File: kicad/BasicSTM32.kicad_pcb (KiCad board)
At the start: 4 copper layers, 61 parts, among them IC1 TPSM53604RDAR, IC2 LD39100PU33R, J1 Screw_Terminal_01x02, J10 Conn_01x04, J11 TC2050-IDC, J2 Conn_01x01, J3 Conn_01x01, J4 Conn_01x02, J5 Conn_01x01, J6 Conn_01x02, J7 DAC1_OUT1, J8 ADC1_IN1, J9 GPIO_OUT PB15, Q1 SI2374DS-T1-GE3, Q2 SI2374DS-T1-GE3, SW1 SW_Push, U1 STM32F303VETx, Y1 NX3225GD-8MHZ-EXS00A-CG04874

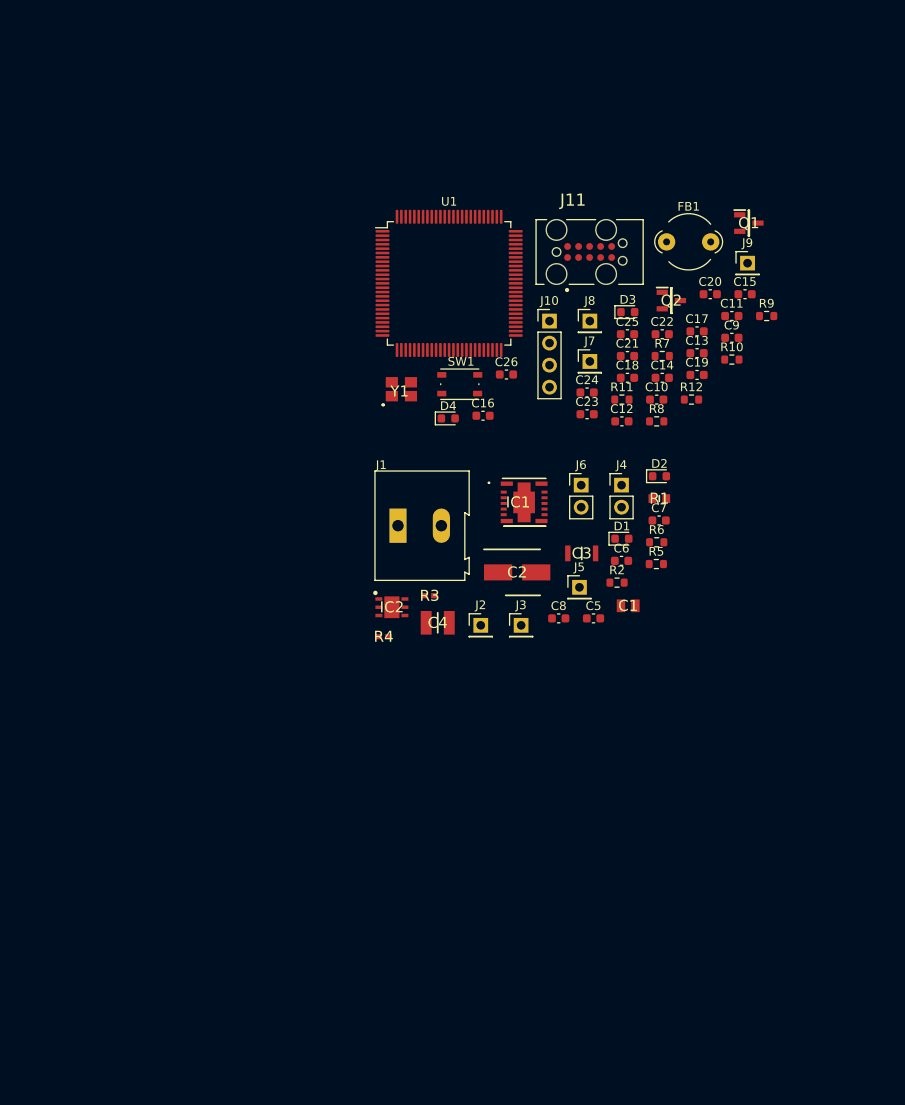
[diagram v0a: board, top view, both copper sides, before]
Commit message: Power supply layout
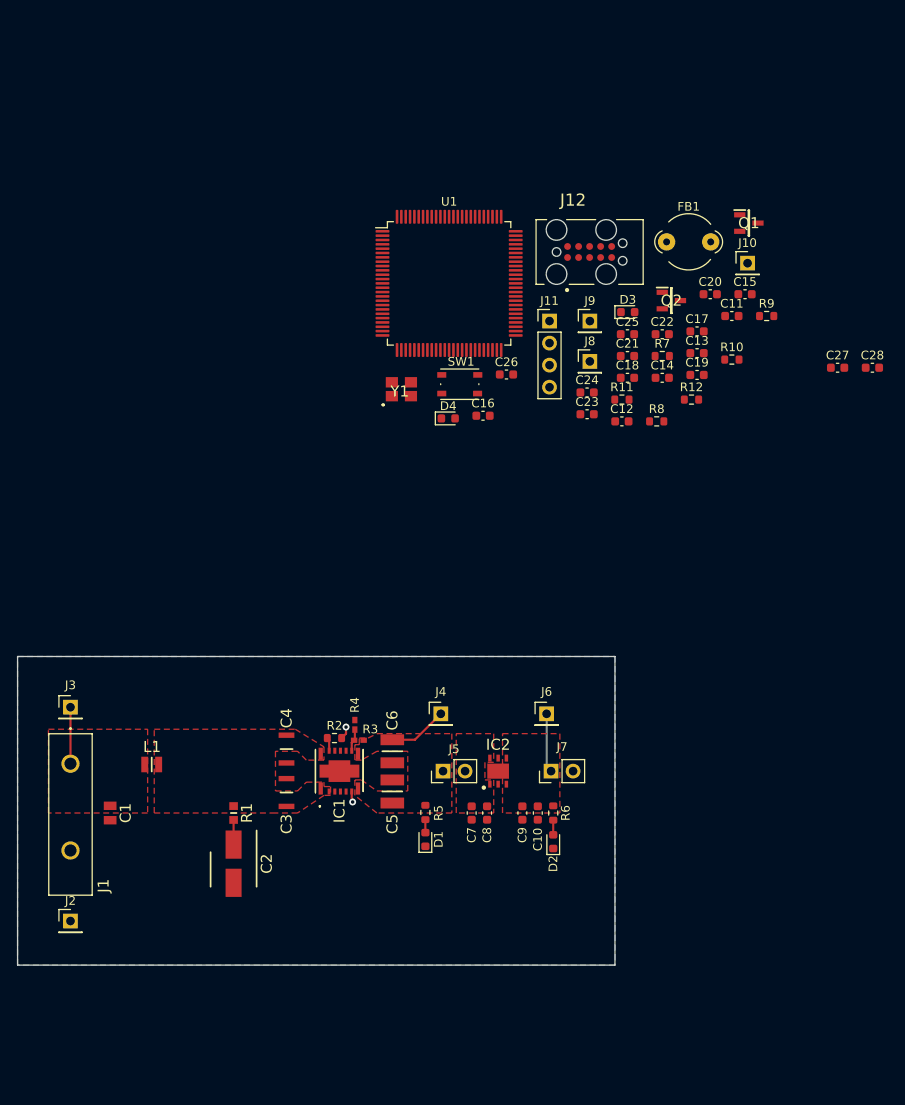
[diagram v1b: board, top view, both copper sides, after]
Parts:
- added C27: 100n, Capacitor_SMD:C_0603_1608Metric, F.Cu at (142.7, 73.4)
- added C28: 1u, Capacitor_SMD:C_0603_1608Metric, F.Cu at (146.8, 73.4)
- added J2: Conn_01x01, Connector_PinHeader_2.54mm:PinHeader_1x01_P2.54mm_Vertical, F.Cu at (54.4, 137.2)
- added L1: DFE201612P-R33M=P2, SamacSys_Parts:1286ASH1R0MP2, F.Cu at (63.7, 119.1)
- C11: value 1u -> 100n
- C12: value 4.7u -> 100n
- C13, C19, C9: value 100n -> 1u
- C14: value 100n -> 4.7u
- C15, C16: value 4.3p -> 100n
- C17, C18: value 1u -> 4.3p
- C4: value GRM32EC81C476KE15L -> C3216X5R1H106K160AB; footprint SamacSys_Parts:CAPC3225X270N -> SamacSys_Parts:CAPC3216X180N
- C5: value 1u -> GRM32EC81C476KE15L; footprint Capacitor_SMD:C_0603_1608Metric -> SamacSys_Parts:CAPC3225X270N
- C6: value 100n -> GRM32EC81C476KE15L; footprint Capacitor_SMD:C_0603_1608Metric -> SamacSys_Parts:CAPC3225X270N
- J1: value Screw_Terminal_01x02 -> 1935161; footprint TerminalBlock:TerminalBlock_Altech_AK300-2_P5.00mm -> SamacSys_Parts:1701023
- moved C1 64.3 mm to (58.9, 124.7), turned to 270 degrees
- moved R1 61.0 mm to (73.2, 124.7), turned to 270 degrees
- moved C9 59.8 mm to (106.4, 124.7), turned to 270 degrees
- moved C10 49.6 mm to (108.2, 124.7), turned to 270 degrees
- moved J3 48.2 mm to (54.4, 112.5)
- moved C2 46.8 mm to (73.2, 130.6), turned to 270 degrees
- moved J1 46.6 mm to (54.4, 119.0), turned to 180 degrees
- moved D2 43.9 mm to (110.0, 128.0), turned to 90 degrees
- moved C3 43.8 mm to (79.2, 122.4), turned to 90 degrees
- moved D1 41.4 mm to (95.2, 127.8), turned to 90 degrees
- moved C7 40.0 mm to (100.6, 124.7), turned to 270 degrees
- moved R5 39.1 mm to (95.2, 124.7), turned to 270 degrees
- moved J5 38.8 mm to (97.3, 119.9), turned to 90 degrees
- moved IC1 38.2 mm to (85.3, 121.9), turned to 90 degrees
- moved R2 37.2 mm to (84.8, 116.1)
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- renumbered J9 to J10, J10 to J11, J11 to J12, J2 to J3, J3 to J4, J4 to J5, J5 to J6, J6 to J7, J7 to J8, J8 to J9
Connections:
- C10 pad 1: /MCU/NRST -> +3V3
- C12 pad 1: VDD -> /MCU/NRST
- C15 pad 1: GND -> VDD
- C15 pad 2: Net-(C15-Pad2) -> GND
- C16 pad 1: Net-(C16-Pad1) -> VDD
- C17 pad 1: VDD -> GND
- C17 pad 2: GND -> Net-(C17-Pad2)
- C18 pad 1: VDD -> Net-(C18-Pad1)
- C25 pad 1: /MCU/VDDA22 -> VDD
- C26 pad 1: /MCU/VDDA22 -> VDD
- C4 pad 1: +5V -> Net-(C3-Pad1)
- C5 pad 1: Net-(C5-Pad1) -> +5V
- C6 pad 1: Net-(C5-Pad1) -> +5V
- C7 pad 1: +3V3 -> Net-(C7-Pad1)
- C8 pad 1: +3V3 -> Net-(C7-Pad1)
- C9 pad 1: VDD -> +3V3
- IC2 pad 1: Net-(C5-Pad1) -> Net-(C7-Pad1)
- IC2 pad 6: Net-(C5-Pad1) -> Net-(C7-Pad1)
- J1 pad 1: GND -> Net-(C1-Pad1)
- J1 pad 2: Net-(C1-Pad1) -> GND
- J5 pad 2: Net-(C5-Pad1) -> Net-(C7-Pad1)
- U1 pad 12: Net-(C15-Pad2) -> Net-(C17-Pad2)
- U1 pad 13: Net-(C16-Pad1) -> Net-(C18-Pad1)
- Y1 pad 1: Net-(C16-Pad1) -> Net-(C18-Pad1)
- Y1 pad 2: Net-(C15-Pad2) -> Net-(C17-Pad2)
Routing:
- net Net-(IC1-Pad6): track 0.00 -> 11.7 mm, vias 0 -> 2
- net +3V3: track 0.00 -> 7.28 mm
- net +5V: track 0.00 -> 6.83 mm
- net Net-(C1-Pad1): track 0.00 -> 6.51 mm
- net Net-(C2-Pad1): track 0.00 -> 2.84 mm
- net Net-(IC1-Pad9): track 0.00 -> 2.58 mm
- net Net-(D2-Pad2): track 0.00 -> 1.69 mm
- net Net-(IC1-Pad13): track 0.00 -> 1.55 mm
- net Net-(D1-Pad2): track 0.00 -> 1.50 mm
- net GND: track 0.00 -> 0.75 mm
- added copper zone on F.Cu, net +3V3
- added copper zone on F.Cu, net +5V
- added copper zone on B.Cu, net GND
- added copper zone on F.Cu, net Net-(C1-Pad1)
- added copper zone on F.Cu, net Net-(C3-Pad1)
- added copper zone on F.Cu, net Net-(C7-Pad1)
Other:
- board outline added: 68.8 x 35.6 mm

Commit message: Start MCU layout
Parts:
- J11: value Conn_01x04 -> S4B-PH-KL_LF__SN_; footprint Connector_PinHeader_2.54mm:PinHeader_1x04_P2.54mm_Vertical -> SamacSys_Parts:S4BPHKLLFSN
- moved J11 45.3 mm to (71.9, 93.2), turned to 90 degrees
- moved C12 44.7 mm to (88.6, 45.8), turned to 180 degrees
- moved C17 40.5 mm to (86.7, 61.6), turned to 270 degrees
- moved C18 33.1 mm to (86.7, 65.4), turned to 270 degrees
- moved J9 29.4 mm to (85.4, 73.9)
- moved SW1 27.7 mm to (88.6, 49.7), turned to 90 degrees
- moved J8 27.5 mm to (88.1, 81.3)
- moved J12 21.6 mm to (98.2, 45.5), turned to 90 degrees
- moved Y1 14.8 mm to (84.3, 63.5), turned to 90 degrees
- moved C1 14.0 mm to (72.9, 125.0)
- moved J1 14.0 mm to (68.3, 119.0)
- moved J2 14.0 mm to (68.3, 137.2)
- moved J3 14.0 mm to (68.3, 112.5)
- moved L1 10.6 mm to (74.3, 119.4)
- moved C2 3.09 mm to (76.2, 131.1)
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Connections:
- J11 pad 2: GND -> Net-(J11-Pad2)
- J11 pad 3: Net-(J11-Pad3) -> VDD
- J11 pad 4: VDD -> GND
- U1 pad 92: Net-(J11-Pad3) -> Net-(J11-Pad2)
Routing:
- net /MCU/NRST: track 0.00 -> 29.8 mm, vias 0 -> 2
- net Net-(C17-Pad2): track 0.00 -> 5.99 mm
- net Net-(C18-Pad1): track 0.00 -> 5.68 mm
- net Net-(J11-Pad2): track 0.00 -> 3.51 mm, vias 0 -> 1
- net Net-(J11-Pad1): track 0.00 -> 3.51 mm, vias 0 -> 1
- net GND: track 0.75 -> 2.65 mm
- net VDD: track 0.00 -> 1.17 mm, vias 0 -> 1
- net Net-(C2-Pad1): track 2.84 -> 3.40 mm

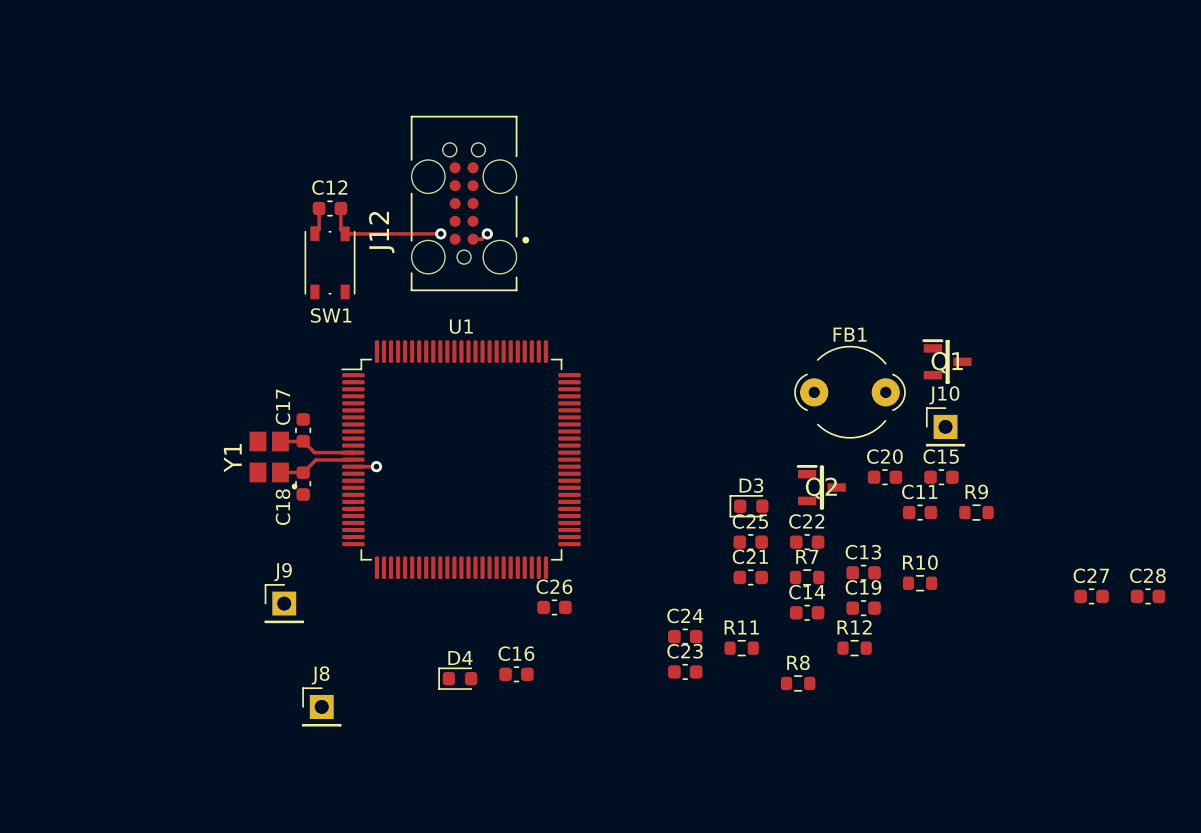
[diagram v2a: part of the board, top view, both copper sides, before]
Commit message: Continue MCU layout
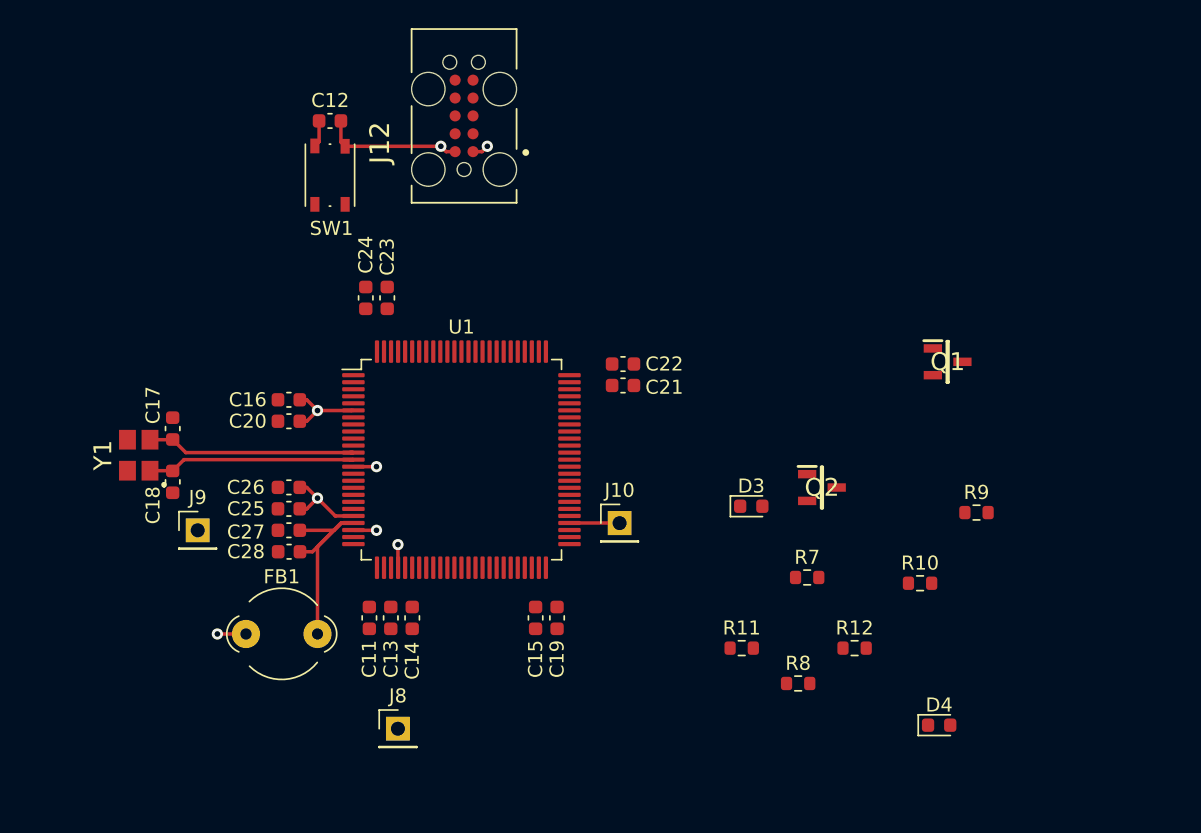
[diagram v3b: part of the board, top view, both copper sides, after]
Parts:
- moved C28 61.1 mm to (85.7, 70.2), turned to 180 degrees
- moved C27 57.2 mm to (85.7, 68.7), turned to 180 degrees
- moved FB1 43.9 mm to (82.7, 76.1)
- moved C20 42.5 mm to (85.7, 61.0), turned to 180 degrees
- moved C11 39.8 mm to (91.4, 74.9), turned to 270 degrees
- moved D4 34.2 mm to (131.9, 82.5)
- moved C23 34.0 mm to (92.7, 52.2), turned to 90 degrees
- moved C13 33.7 mm to (93.0, 74.9), turned to 270 degrees
- moved C24 33.1 mm to (91.2, 52.2), turned to 90 degrees
- moved C25 32.9 mm to (85.7, 67.2), turned to 180 degrees
- moved C15 30.5 mm to (103.3, 74.9), turned to 270 degrees
- moved C14 28.1 mm to (94.5, 74.9), turned to 270 degrees
- moved C16 25.3 mm to (85.7, 59.4), turned to 180 degrees
- moved J10 24.1 mm to (109.2, 68.2)
- moved C19 21.8 mm to (104.8, 74.9), turned to 270 degrees
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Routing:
- net /MCU/VDDA22: track 0.00 -> 16.4 mm
- net Net-(J8-Pad1): track 0.00 -> 14.7 mm, vias 0 -> 1
- net Net-(J9-Pad1): track 0.00 -> 14.3 mm, vias 0 -> 1
- net VDD: track 1.17 -> 15.1 mm, vias 1 -> 4
- net Net-(C18-Pad1): track 5.68 -> 15.1 mm
- net Net-(C17-Pad2): track 5.99 -> 15.3 mm
- net /MCU/NRST: track 29.8 -> 37.1 mm
- net Net-(J10-Pad1): track 0.00 -> 3.57 mm

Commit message: Finish layout first pass
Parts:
- moved Q1 68.2 mm to (88.4, 108.7), turned to 270 degrees
- moved R9 64.3 mm to (88.4, 112.1), turned to 90 degrees
- moved J12 59.4 mm to (108.4, 97.8), turned to 0 degrees
- moved D3 56.9 mm to (88.4, 115.2), turned to 270 degrees
- moved C12 55.2 mm to (114.0, 88.6), turned to 90 degrees
- moved C22 53.3 mm to (95.9, 108.4), turned to 270 degrees
- moved C21 52.3 mm to (94.4, 108.4), turned to 270 degrees
- moved SW1 50.0 mm to (110.2, 88.6), turned to 0 degrees
- moved R7 47.1 mm to (91.7, 107.7), turned to 180 degrees
- moved J10 47.0 mm to (84.6, 108.2), turned to 270 degrees
- moved Q2 45.5 mm to (100.6, 104.9), turned to 270 degrees
- moved D4 42.6 mm to (100.6, 111.4), turned to 270 degrees
- moved C23 40.4 mm to (101.1, 91.7), turned to 0 degrees
- moved R10 40.0 mm to (107.8, 105.4)
- moved C19 39.8 mm to (77.3, 103.8), turned to 180 degrees
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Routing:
- net VDD: track 15.1 -> 47.2 mm, vias 4 -> 12
- net Net-(J12-Pad4): track 0.01 -> 24.2 mm, vias 0 -> 2
- net Net-(J11-Pad2): track 3.51 -> 27.6 mm
- net Net-(J11-Pad1): track 3.51 -> 27.3 mm
- net Net-(J12-Pad2): track 0.00 -> 23.3 mm, vias 0 -> 2
- net /MCU/NRST: track 37.1 -> 54.1 mm, vias 2 -> 3
- net GND: track 2.65 -> 15.9 mm, vias 0 -> 3
- net Net-(Q2-Pad1): track 0.00 -> 7.09 mm
- net Net-(Q1-Pad1): track 0.00 -> 5.08 mm
- net Net-(IC1-Pad6): track 11.7 -> 14.5 mm
- net Net-(Q1-Pad3): track 0.00 -> 1.55 mm
- net Net-(Q2-Pad3): track 0.00 -> 1.55 mm
- net Net-(D3-Pad1): track 0.00 -> 1.46 mm
- net Net-(D4-Pad1): track 0.00 -> 1.46 mm
- net Net-(C3-Pad1): track 0.00 -> 1.12 mm
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- added copper zone on F.Cu, net GND
- added copper zone on GND, net GND
- added copper zone on F.Cu, net VDD
- added copper zone on VDD, net VDD
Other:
- board size 68.8 x 35.6 mm -> 64.3 x 83.2 mm

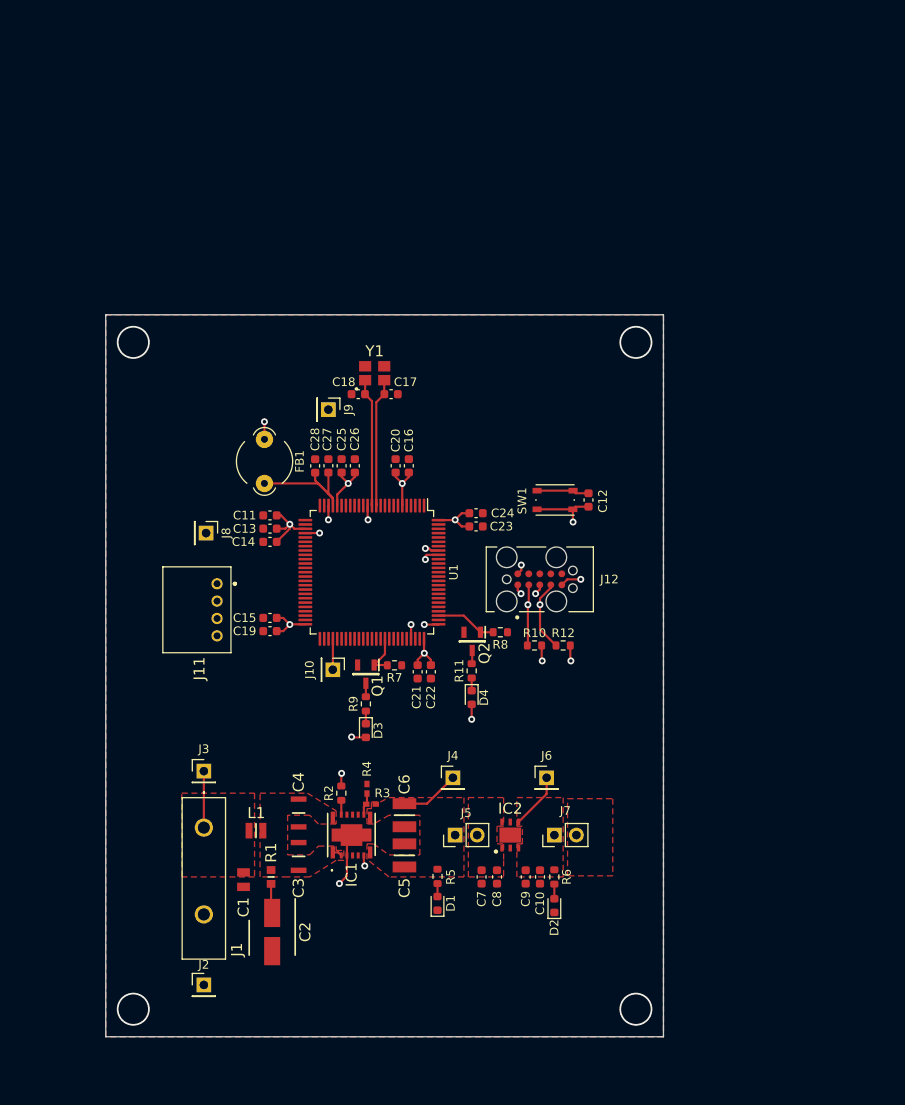
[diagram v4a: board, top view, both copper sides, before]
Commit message: Add USB
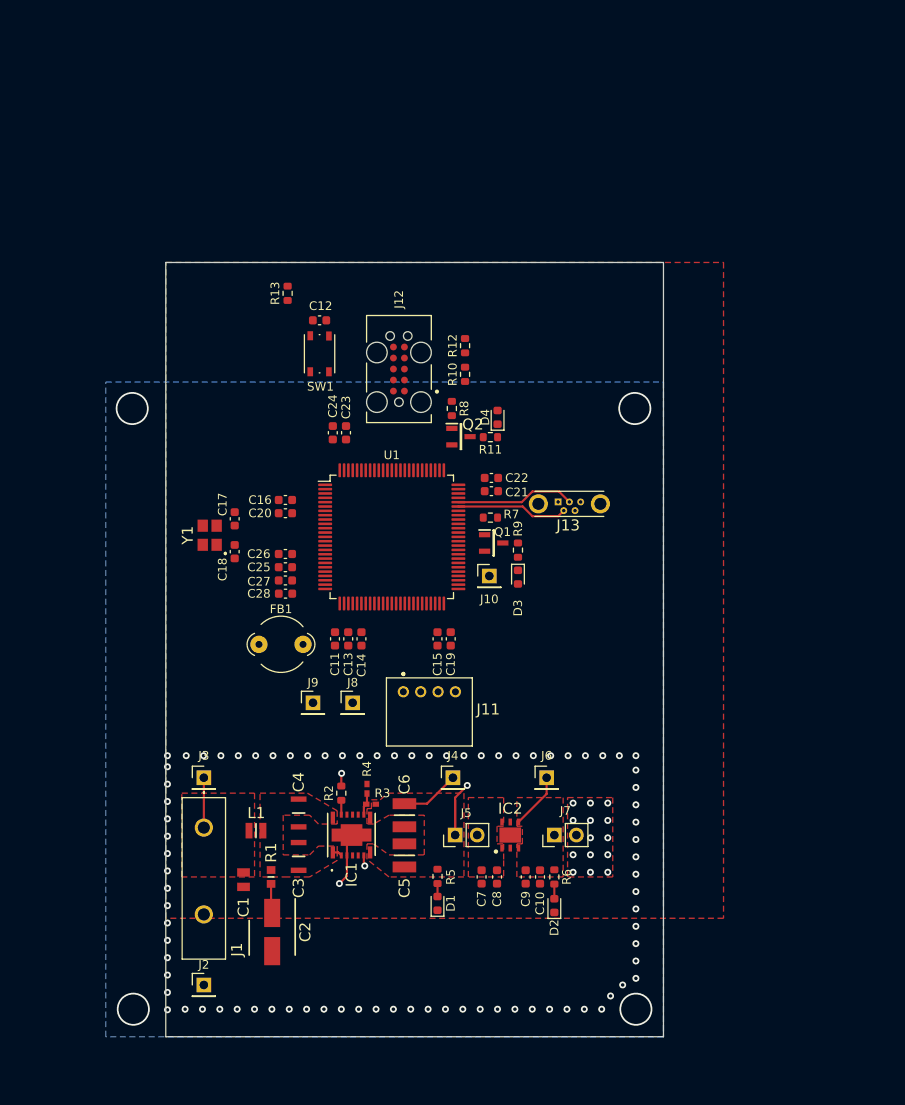
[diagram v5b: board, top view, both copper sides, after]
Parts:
- added J13: USB3131-30-0230-A, SamacSys_Parts:USB3131300230A, F.Cu at (110.5, 88.9)
- added R13: 1k5, Resistor_SMD:R_0603_1608Metric, F.Cu at (79.4, 64.8)
- moved C12 37.3 mm to (83.1, 67.9), turned to 180 degrees
- moved R12 36.3 mm to (99.8, 70.9), turned to 90 degrees
- moved J9 33.8 mm to (82.3, 112.0), turned to 0 degrees
- moved D4 32.4 mm to (103.6, 79.1), turned to 90 degrees
- moved R10 32.3 mm to (99.8, 74.2), turned to 90 degrees
- moved SW1 31.9 mm to (83.1, 71.8), turned to 90 degrees
- moved J12 29.2 mm to (92.2, 73.6), turned to 90 degrees
- moved R11 27.0 mm to (102.7, 81.4), turned to 180 degrees
- moved Y1 26.6 mm to (70.4, 92.7), turned to 90 degrees
- moved R8 26.4 mm to (98.3, 78.1), turned to 270 degrees
- moved J8 25.8 mm to (86.9, 112.0), turned to 0 degrees
- moved R9 24.9 mm to (105.9, 94.4)
- moved D3 24.9 mm to (105.9, 97.5)
- moved J11 24.8 mm to (92.7, 110.7), turned to 180 degrees
- moved FB1 23.6 mm to (76.1, 105.3), turned to 0 degrees
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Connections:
- U1 pad 70: GND -> /MCU/USB_N
- U1 pad 71: GND -> /MCU/USB_P
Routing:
- net /MCU/NRST: track 54.1 -> 0.00 mm, vias 3 -> 0
- net +5V: track 6.83 -> 58.6 mm, vias 0 -> 1
- net VDD: track 47.2 -> 0.00 mm, vias 12 -> 14
- net Net-(J11-Pad2): track 27.6 -> 0.00 mm, vias 1 -> 0
- net Net-(J11-Pad1): track 27.3 -> 0.00 mm, vias 1 -> 0
- net Net-(J12-Pad4): track 24.2 -> 0.00 mm, vias 2 -> 0
- net Net-(J12-Pad2): track 23.3 -> 0.00 mm, vias 2 -> 0
- net /MCU/VDDA22: track 16.4 -> 0.00 mm
- net Net-(C17-Pad2): track 15.3 -> 0.00 mm
- net Net-(C18-Pad1): track 15.1 -> 0.00 mm
- net Net-(J8-Pad1): track 14.7 -> 0.00 mm, vias 1 -> 0
- net Net-(J9-Pad1): track 14.3 -> 0.00 mm, vias 1 -> 0
- net /MCU/USB_P: track 0.00 -> 13.8 mm
- net /MCU/USB_N: track 0.00 -> 12.9 mm
- net GND: track 15.9 -> 6.18 mm, vias 3 -> 84
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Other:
- board size 64.3 x 83.2 mm -> 57.3 x 89.2 mm
- net class USB added: clearance 0.2, trace_width 0.25, via_dia 0.8, via_drill 0.4
